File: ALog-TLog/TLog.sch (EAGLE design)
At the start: 94 parts, among them IC1 ATMEGA644M, J6 5.5x2.1mm Barrel, Q1 220mA/50V/3.5Ω, Q5 4.3A/20V/54mΩ, Q6 4.3A/20V/54mΩ, Q7 4.3A/20V/54mΩ, Q8 220mA/50V/3.5Ω, Q9 220mA/50V/3.5Ω, U2 FT231X-Q, U3 915MHz, U4 SX1509

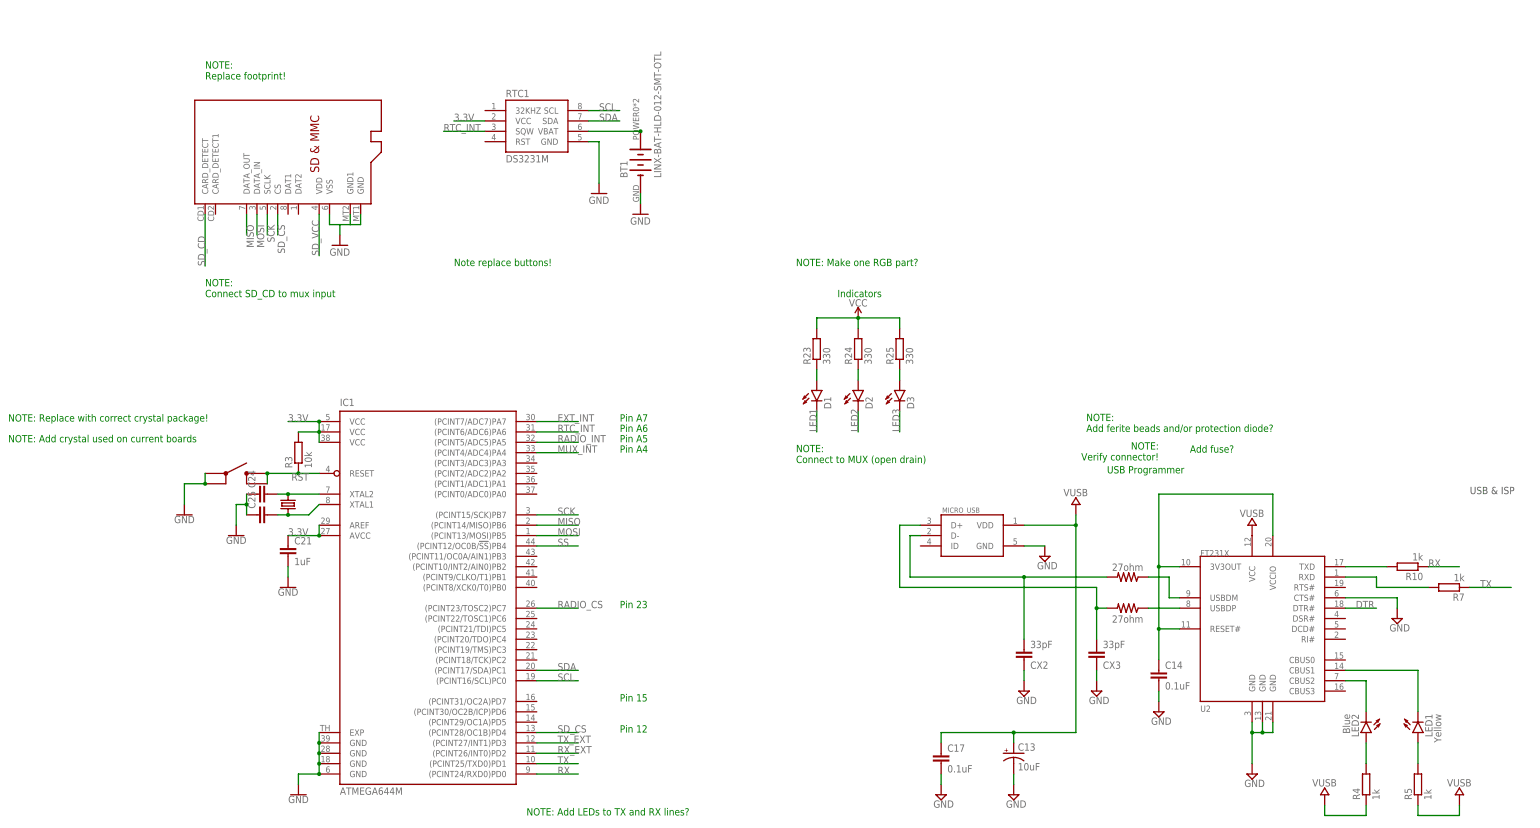
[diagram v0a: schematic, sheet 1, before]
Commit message: TLog Board Ready for Review
TLog board is at functional stage and ready for review by general eyes, High Speed ADC daughter board preliminary files also added (location may change eventually)
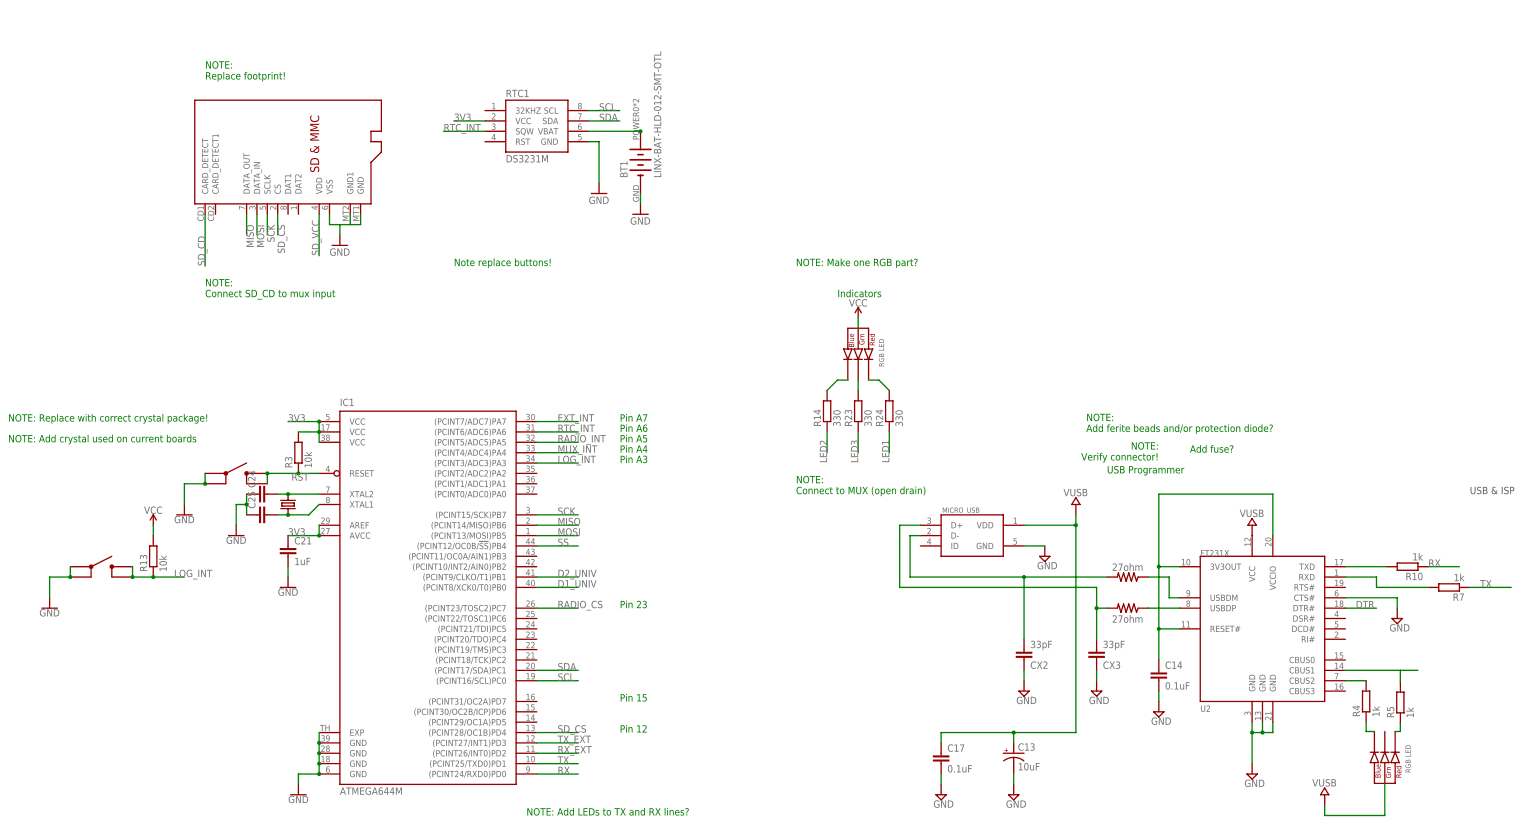
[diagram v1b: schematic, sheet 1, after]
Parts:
- removed D1, D2, D3: (no value), SparkFun-LED:LED0603
- removed LED1: Yellow, SparkFun-LED:LED0603
- removed LED2: Blue, SparkFun-LED:LED0603
- removed R25: 330, rcl:R-EU_R0603
- added R13: 10k, resistor:R-EU_R0603
- added R14: 330, resistor:R-EU_R0603
- added U$15, U$16: CLVBA-FKA, bschulz:CLVBA-FKA
- added U$5: SKRPABE010, Custom:SKRPABE010
- added X2: 87832-14, con-molex:87832-14
- R23, R24: device rcl:R-EU_R0603 -> resistor:R-EU_R0603
- R6: value 10k -> (none)
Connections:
- removed net 3.3V: C10.1, C21.1, C3.1, IC1.AREF, IC1.AVCC, IC1.VCC, IC1.VCC@1, IC1.VCC@2, J1.2, J2.2, L2.P$2, Q1.G, Q5.S, Q7.S, Q8.G, Q9.G, R11.2, R12.2, R23.2, R24.2, R25.2, R3.2, R42.2, R43.2, R6.2, RTC1.VCC, U$4.SLEEP, U$4.VOS, U$6.VCC, U$6.VCC_IO, U$6.V_BCKP, U3.3.3V, U4.VCC1, U4.VCC2, U4.VDDM
- removed net N$32: D1.A, R23.1
- removed net N$33: D2.A, R24.1
- removed net N$34: D3.A, R25.1
- removed net N$40: LED2.A, R4.2
- removed net N$42: LED1.A, R5.2
- new net 3V3: C10.1, C21.1, C3.1, IC1.AREF, IC1.AVCC, IC1.VCC, IC1.VCC@1, IC1.VCC@2, J1.2, J2.2, L2.P$2, Q5.S, Q7.S, Q8.G, Q9.G, R11.2, R12.2, R13.2, R3.2, R42.2, R43.2, R6.2, RTC1.VCC, U$15.ANODE, U$4.SLEEP, U$4.VOS, U$6.VCC, U$6.VCC_IO, U$6.V_BCKP, U3.3.3V, U4.VCC1, U4.VCC2, U4.VDDM
- new net D1_UNIV: IC1.(PCINT8/XCK0/T0)PB0, X2.5
- new net D2_UNIV: IC1.(PCINT9/CLKO/T1)PB1, X2.14
- new net LOG_INT: IC1.(PCINT3/ADC3)PA3, R13.1, U$5.3, U$5.4
- new net N$10: R23.2, U$15.GREEN_CATH
- new net N$15: R24.2, U$15.RED_CATH
- new net N$16: R5.1, U$16.RED_CATH
- new net N$26: R4.1, U$16.BLUE_CATH
- new net N$9: R14.2, U$15.BLUE_CATH
- net 5V: now also R21.1
- net 5V_EXT_CTRL: now also Q1.G; no longer Q1.S
- net ADC5: now also X2.12
- net ADC6: now also X2.13
- net EXT_3.3V: now also X2.2
- net EXT_5V: now also X2.3
- net GND: now also Q1.S, U$5.1, U$5.2, X2.1; no longer R21.1
- net LED1: now also R24.1; no longer D1.C
- net LED2: now also R14.1; no longer D2.C
- net LED3: now also R23.1; no longer D3.C
- net MISO: now also X2.6
- net MOSI: now also X2.9
- net N$41: now also R4.2; no longer LED2.C
- net N$43: now also R5.2; no longer LED1.C
- net RX_EXT: now also X2.7
- net SCK: now also X2.10
- net SCL: now also X2.11
- net SDA: now also X2.4
- net TX_EXT: now also X2.8
- net VUSB: now also U$16.ANODE; no longer R4.1, R5.1
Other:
- note added: "Pin A3"
- moved on the sheet: R23, R24, R4, R5, R6

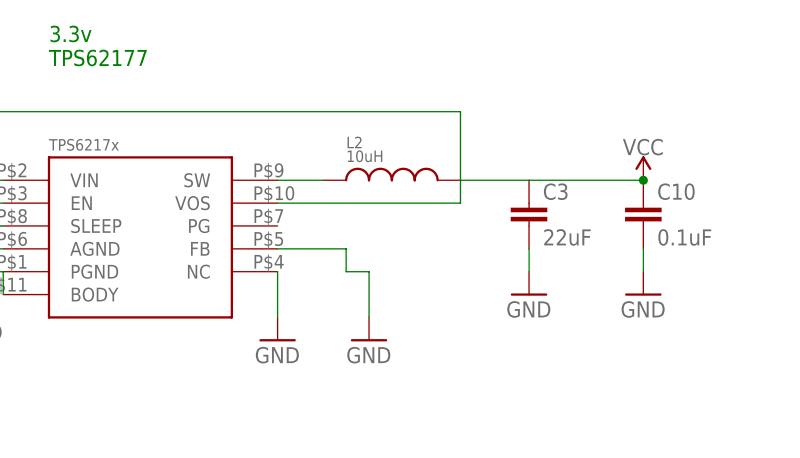
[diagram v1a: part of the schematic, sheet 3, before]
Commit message: In Progress of modifying board for auto BOM
Working on cleaning up the board and libraries such that an auto BOM can be formed, also beginning to clean up silk screen for first run of PCBs
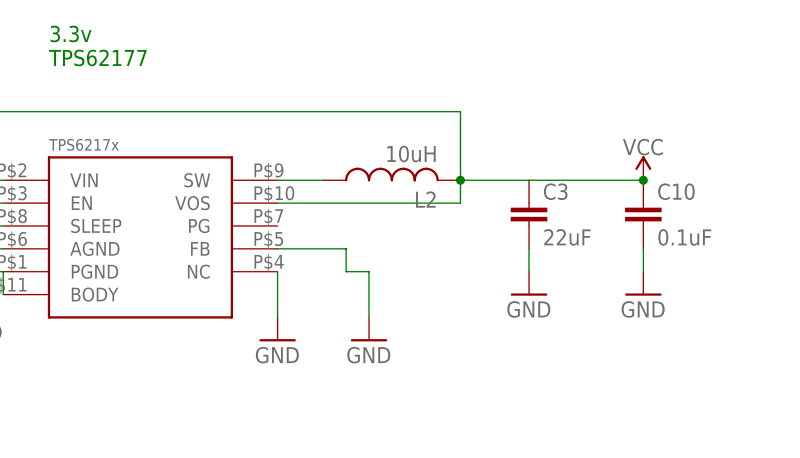
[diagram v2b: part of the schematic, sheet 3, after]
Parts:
- IC1: device atmel:ATMEGA644M -> bschulz:ATMEGA644M
- J10, J5, J8, J9: device SparkFun-Connectors:CONN_10 -> bschulz:CONN_103.5MM
- L2: device Custom:WE-LSQ(INDUCTOR) -> bschulz:INDUCTORLQS_4X4
- Q5, Q6, Q7: value 4.3A/20V/54mΩ -> MOSFET_PCH-IRLML2244; device SparkFun-DiscreteSemi:MOSFET_PCH-IRLML2244 -> bschulz:MOSFET_PCH-IRLML2244
- Q8, Q9: value 220mA/50V/3.5Ω -> MOSFET-NCH-BSS138; device SparkFun-DiscreteSemi:MOSFET-NCH-BSS138 -> bschulz:MOSFET-NCH-BSS138
- R13, R3: DIGIKEY (none) -> 311-10.0KHRCT-ND
- RTC1: device SparkFun-Clocks:DS3231M -> bschulz:DS3231M
- U$10: value MAX6070 -> MAX6070AAUT18; device bschulz:MAX6070 -> bschulz:MAX6070AAUT18
- U$2: device adafruit:MICROSD -> bschulz:MICROSD
- U$3: device Custom:TPS306X -> bschulz:TPS3060
- U$4: value TPS6217X -> TPS6217XTPS62177; device texas:TPS6217X -> bschulz:TPS6217XTPS62177
- U$5, U$9: device Custom:SKRPABE010 -> bschulz:SKRPABE010
- U$7: device linear-technology:LTC2495 -> bschulz:LTC2495
- U$8: device Custom:WE-MAIA(INDUCTOR) -> bschulz:INDUCTORMAIA_4.1X4.1
- U4: device SparkFun-IC-Special-Function:SX1509 -> bschulz:SX1509
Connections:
- net 3V3: now also L2.2; no longer L2.P$2
- net N$2: now also L2.1; no longer L2.P$1

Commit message: Fixed silk screen and capacitor size
Fixed the silk screen layout and changed capacitor sizes on the buck-boost converter (From all 0603 to some 0805 and some 1206)
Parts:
- C19, C26, C27: device rcl:C-EUC0603 -> rcl:C-EUC1206
- C2: device rcl:C-EUC0603 -> rcl:C-EUC0805
- C3: device rcl:C-EUC1210 -> rcl:C-EUC1206
- MICRO_USB: value 10118194-0001LF_LONGER_PADS -> MICRO_USB_LONGPADS; device 10118194-0001LF:10118194-0001LF_LONGER_PADS -> bschulz:MICRO_USB_LONGPADS

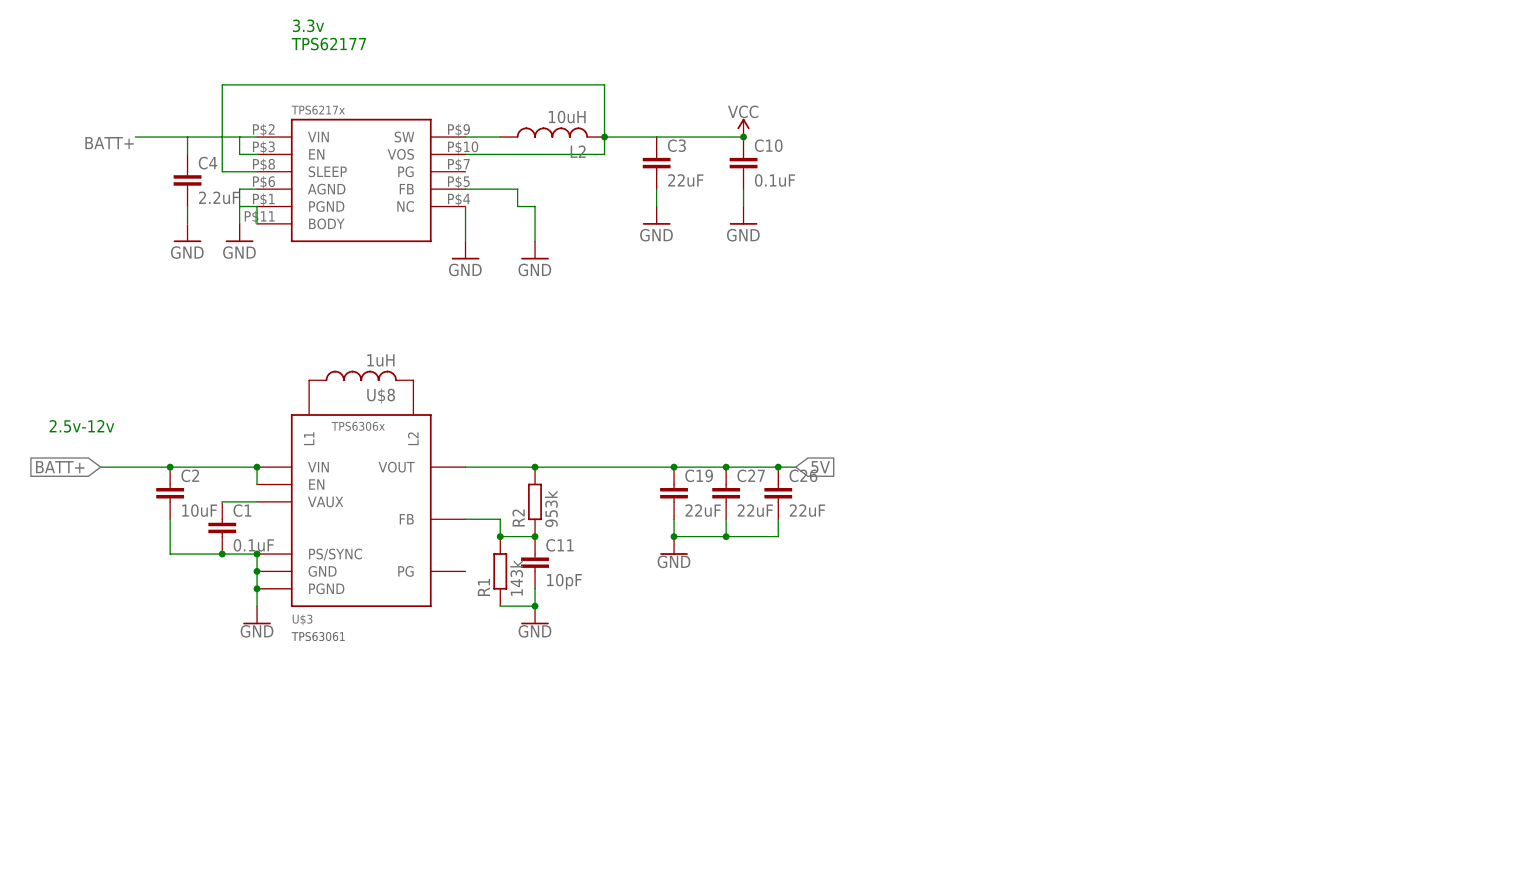
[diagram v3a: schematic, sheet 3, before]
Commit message: updated 5V regulator footprint, trace fixes
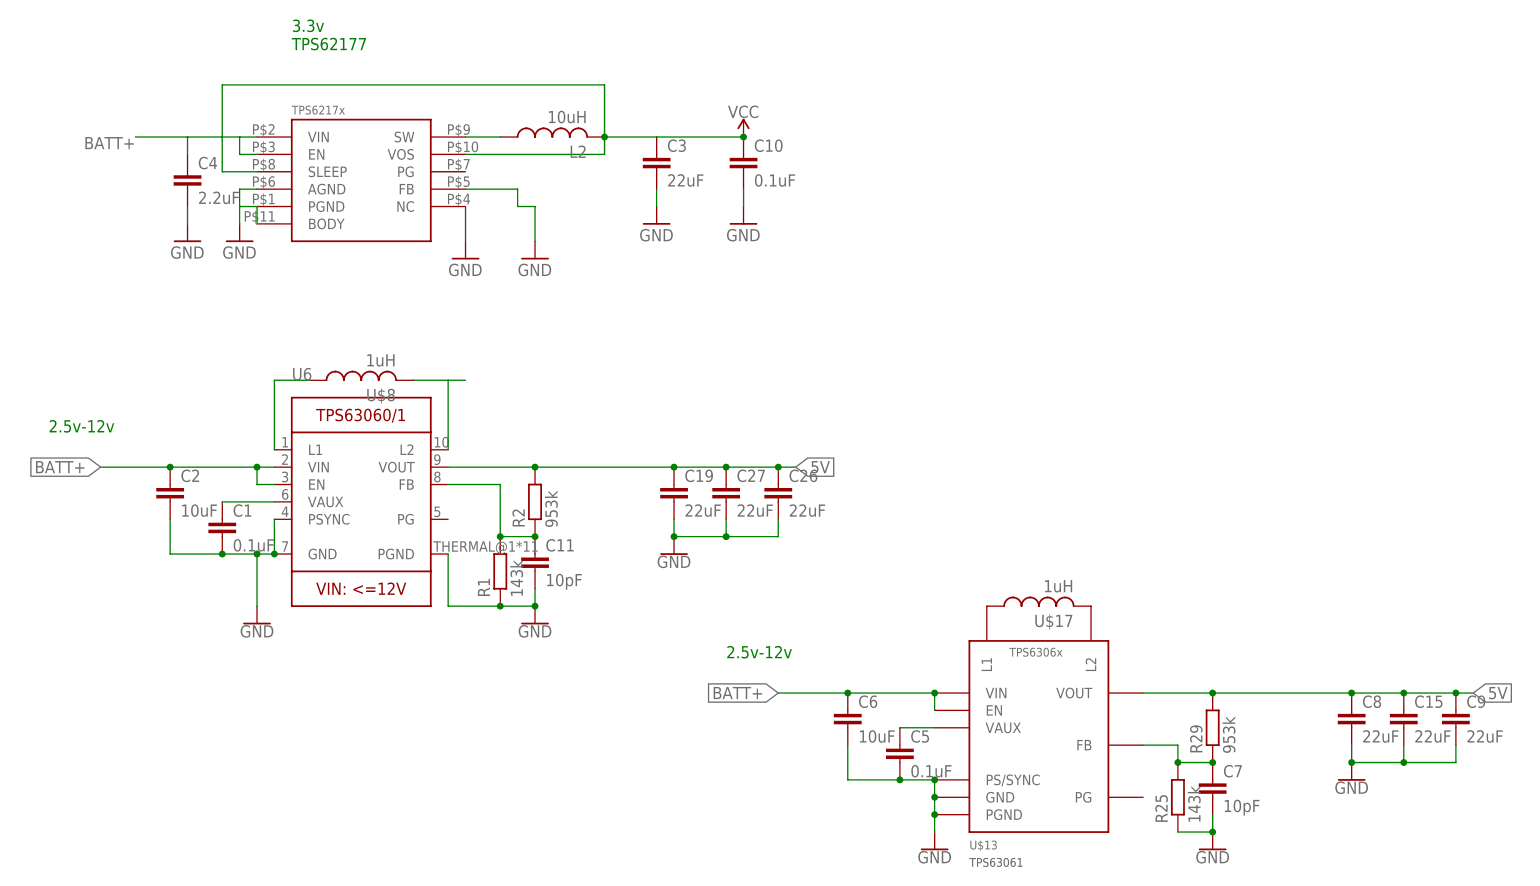
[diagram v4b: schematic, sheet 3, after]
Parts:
- removed U$3: TPS63061, bschulz:TPS3060
- added C15, C8, C9: 22uF, rcl:C-EUC1206
- added C5: 0.1uF, rcl:C-EUC0603
- added C6: 10uF, rcl:C-EUC0805
- added C7: 10pF, rcl:C-EUC0603
- added R25: 143k, rcl:R-EU_R0603
- added R29: 953k, rcl:R-EU_R0603
- added U$13: TPS63061, bschulz:TPS3060
- added U$17: 1uH, bschulz:INDUCTORMAIA_4.1X4.1
- added U1, U5, U6: (no value), microbuilder:VREG_TPS63060/1
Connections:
- removed net N$1: U$3.L2, U$8.2
- removed net N$3: U$3.L1, U$8.1
- new net N$29: U5.L2
- new net N$32: U$8.1, U6.L1
- new net N$33: U$13.L2, U$17.2
- new net N$34: U$13.L1, U$17.1
- new net N$40: C5.1, U$13.VAUX
- new net N$42: C7.1, R25.2, R29.1, U$13.FB
- new net N$47: U$8.2, U6.L2
- net 5V: now also C15.1, C8.1, C9.1, R29.2, U$13.VOUT, U6.VOUT; no longer U$3.VOUT
- net BATT+: now also C6.1, U$13.EN, U$13.VIN, U6.EN, U6.VIN; no longer U$3.EN, U$3.VIN
- net GND: now also C15.2, C5.2, C6.2, C7.2, C8.2, C9.2, R25.1, U$13.GND, U$13.PGND, U$13.PS/SYNC, U6.GND, U6.PGND, U6.PSYNC; no longer U$3.GND, U$3.PGND, U$3.PS/SYNC
- net N$4: now also U6.VAUX; no longer U$3.VAUX
- net N$6: now also U6.FB; no longer U$3.FB

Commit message: updated 3.3V regulator
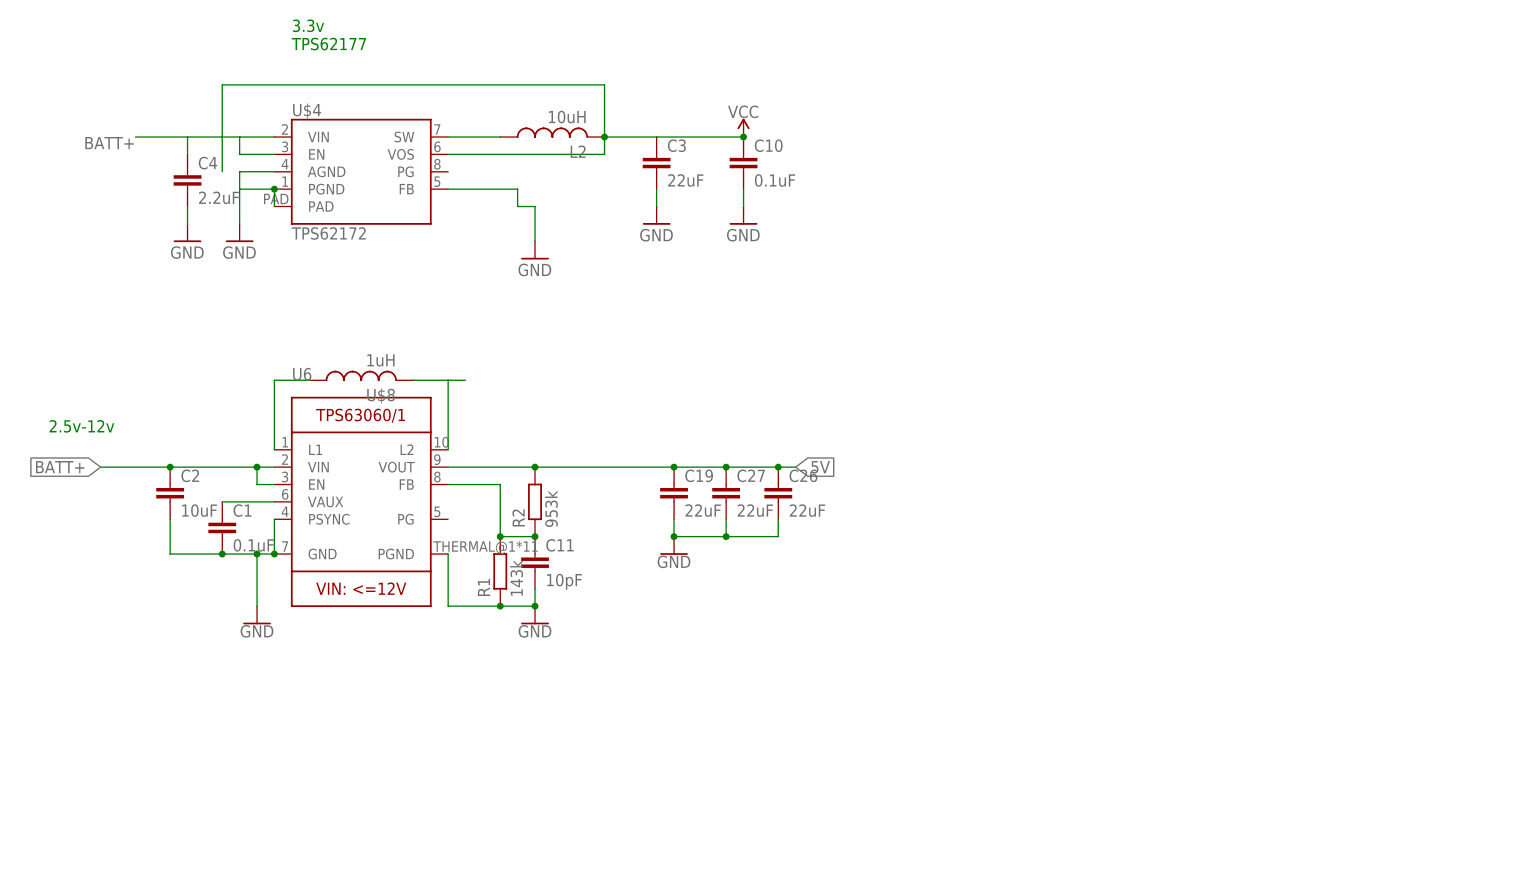
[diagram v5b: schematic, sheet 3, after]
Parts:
- removed C15, C8, C9: 22uF, rcl:C-EUC1206
- removed C5: 0.1uF, rcl:C-EUC0603
- removed C6: 10uF, rcl:C-EUC0805
- removed C7: 10pF, rcl:C-EUC0603
- removed R25: 143k, rcl:R-EU_R0603
- removed R29: 953k, rcl:R-EU_R0603
- removed U$13: TPS63061, bschulz:TPS3060
- removed U$17: 1uH, bschulz:INDUCTORMAIA_4.1X4.1
- removed U1, U5: (no value), microbuilder:VREG_TPS63060/1
- U$4: value TPS6217XTPS62177 -> TPS62172; device bschulz:TPS6217XTPS62177 -> SparkFun-IC-Power:TPS62172
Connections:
- removed net N$29: U5.L2
- removed net N$33: U$13.L2, U$17.2
- removed net N$34: U$13.L1, U$17.1
- removed net N$40: C5.1, U$13.VAUX
- removed net N$42: C7.1, R25.2, R29.1, U$13.FB
- net 3V3: no longer U$4.SLEEP
- net 5V: no longer C15.1, C8.1, C9.1, R29.2, U$13.VOUT
- net BATT+: no longer C6.1, U$13.EN, U$13.VIN
- net GND: now also U$4.PAD; no longer C15.2, C5.2, C6.2, C7.2, C8.2, C9.2, R25.1, U$13.GND, U$13.PGND, U$13.PS/SYNC, U$4.BODY, U$4.NC
